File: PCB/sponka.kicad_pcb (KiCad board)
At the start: 2 copper layers, 87.2 x 10.9 mm, 29 parts, among them J1 Conn_01x03_Pin, J2 USB_C_Receptacle_USB2.0_14P, J3 Conn_01x02_Socket, J4 Conn_01x05_Pin, SW1 SW_Push, SW2 SW_SPDT, U1 CH32V003FxUx, U2 TP4057, U3 AP2127K-3.3

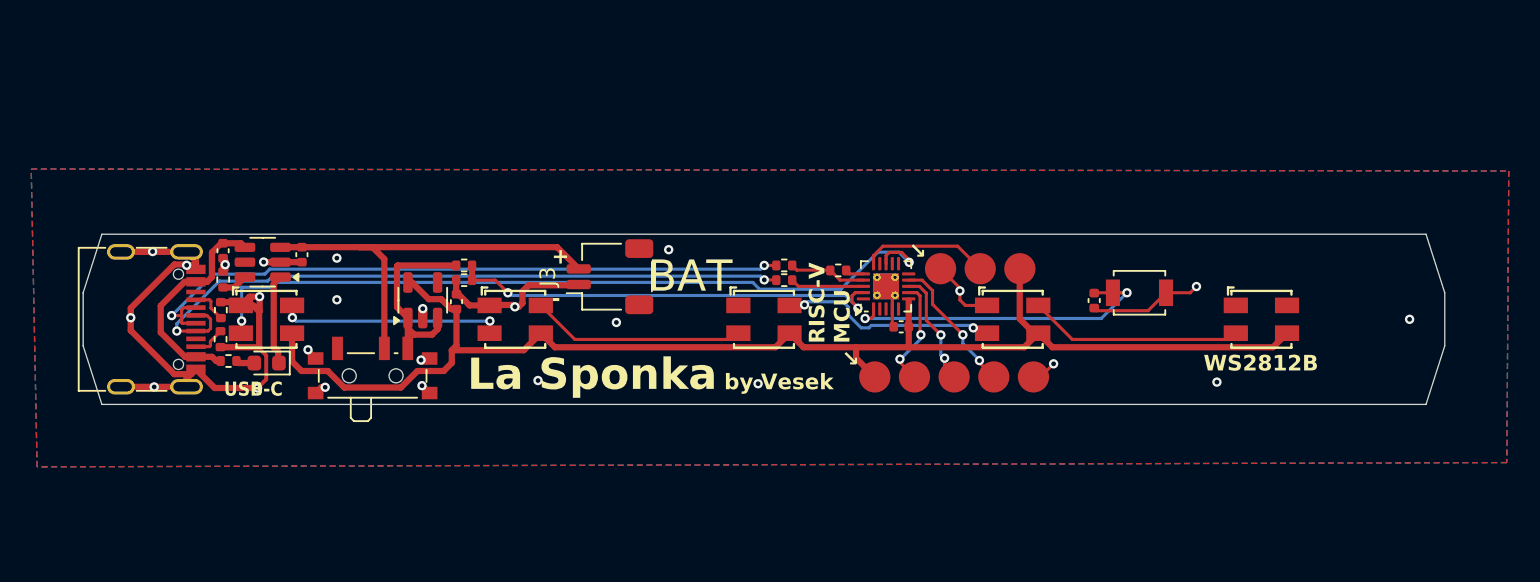
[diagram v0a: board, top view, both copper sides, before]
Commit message: Add protection circuit to PCB I don't like the design tho, so let's fix that
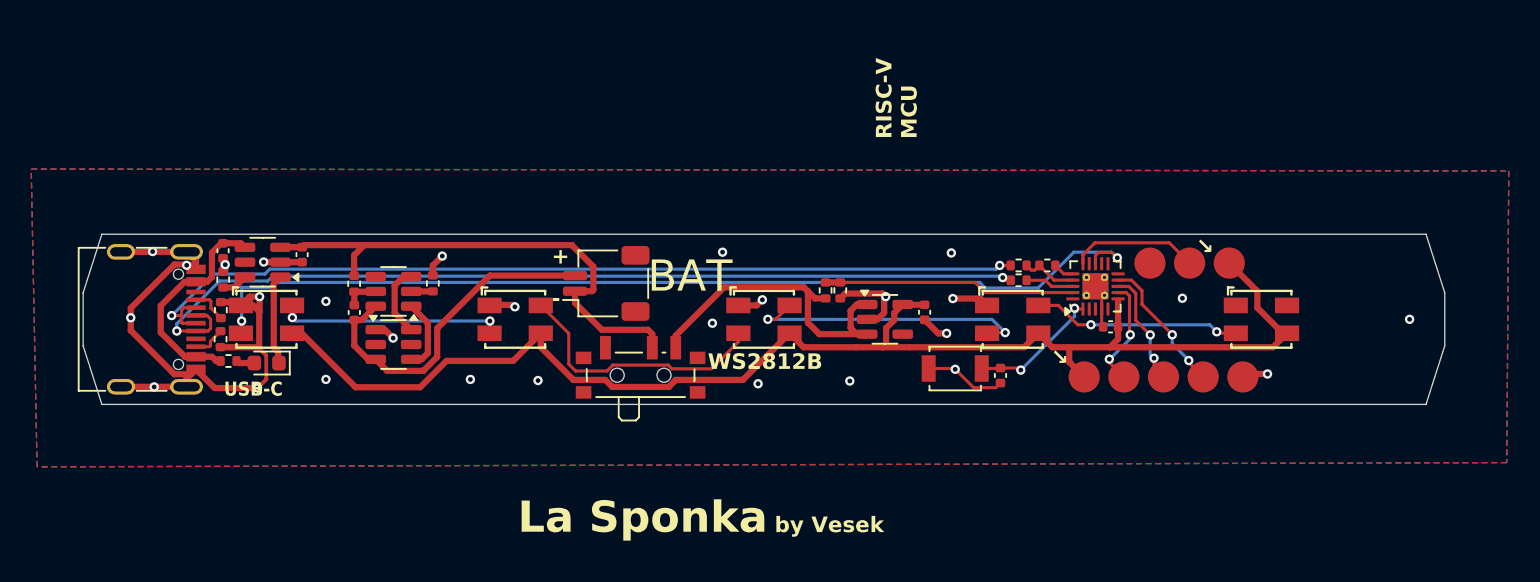
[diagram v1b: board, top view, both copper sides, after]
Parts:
- added C6: 100nF, Capacitor_SMD:C_0402_1005Metric, F.Cu at (118.1, 100.9)
- added Q1: FS8205, Package_TO_SOT_SMD:SOT-23-6, F.Cu at (120.6, 103.0)
- added R10: 100, Resistor_SMD:R_0402_1005Metric, F.Cu at (118.1, 99.1)
- added R11: 1k, Resistor_SMD:R_0402_1005Metric, F.Cu at (123.1, 99.1)
- added U4: DW01A, Package_TO_SOT_SMD:SOT-23-6, F.Cu at (120.6, 99.6)
- moved C5 30.0 mm to (154.6, 100.9), turned to -90 degrees
- moved U3 29.6 mm to (152.1, 101.3), turned to 0 degrees
- moved R8 24.1 mm to (149.2, 99.5), turned to -90 degrees
- moved R7 23.2 mm to (148.2, 99.5), turned to 90 degrees
- moved SW2 17.2 mm to (136.4, 104.6)
- moved R4 15.0 mm to (160.6, 98.8)
- moved R3 15.0 mm to (160.6, 97.9)
- moved J1 13.4 mm to (171.6, 97.8)
- moved C1 13.4 mm to (166.5, 101.8)
- moved J4 13.4 mm to (169.8, 105.0)
- moved U1 13.4 mm to (165.5, 99.2)
- moved R9 13.4 mm to (162.4, 97.9)
- moved SW1 12.8 mm to (156.6, 104.5), turned to 180 degrees
- moved C2 7.68 mm to (159.4, 105.0)
- moved J3 0.49 mm to (134.2, 99.0)
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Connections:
- C4 pad 1: GND -> /Power management/B+
- C4 pad 2: Net-(J3-Pin_2) -> GND
- J3 pad 1: GND -> /Power management/B+
- J3 pad 2: Net-(J3-Pin_2) -> /Power management/B-
- SW2 pad : GND -> (no net)
- SW2 pad 2: Net-(J3-Pin_2) -> /Power management/B+
- U2 pad 3: Net-(J3-Pin_2) -> /Power management/B+
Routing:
- net /Power management/B+: track 0.00 -> 33.0 mm
- net Net-(J3-Pin_2): track 27.3 -> 0.00 mm
- net /Power management/B-: track 0.00 -> 21.8 mm
- net /Power management/DP: track 44.2 -> 59.2 mm
- net /Power management/DN: track 43.4 -> 58.5 mm
- net Net-(U1-PD7): track 21.5 -> 8.51 mm
- net /LED Row/Row_DIN: track 49.7 -> 62.6 mm
- net /Power management/BATT_DIV: track 28.2 -> 16.1 mm, vias 2 -> 0
- net Net-(SW2-C): track 13.0 -> 21.6 mm
- net Net-(Q1-G2): track 0.00 -> 4.67 mm
- net Net-(Q1-G1): track 0.00 -> 4.57 mm
- net Net-(LED3-DOUT): track 14.0 -> 18.5 mm
- net GND: track 77.3 -> 73.1 mm, vias 25 -> 27
- net Net-(LED2-DOUT): track 13.7 -> 17.1 mm
- net Net-(U4-VCC): track 0.00 -> 2.24 mm
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
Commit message: Probably done?
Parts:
- moved LED1 63.7 mm to (176.2, 101.3), turned to 0 degrees
- moved LED5 63.7 mm to (112.5, 101.3), turned to 0 degrees
- moved LED2 31.9 mm to (160.2, 101.3), turned to 0 degrees
- moved LED4 31.9 mm to (128.4, 101.3), turned to 0 degrees
- moved J1 18.9 mm to (152.7, 97.5)
- moved J3 16.6 mm to (118.3, 103.9)
- moved C5 15.2 mm to (139.5, 100.0)
- moved U3 15.2 mm to (136.9, 100.5)
- moved R3 12.8 mm to (148.4, 101.8)
- moved R4 12.8 mm to (148.4, 102.8)
- moved R9 12.8 mm to (150.2, 101.8)
- moved C1 12.7 mm to (154.3, 105.5)
- moved U1 12.7 mm to (153.3, 102.9)
- moved SW1 12.5 mm to (168.8, 102.0), turned to 0 degrees
- moved J4 7.60 mm to (162.2, 105.2)
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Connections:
- SW2 pad : (no net) -> GND
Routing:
- net /Power management/DP: track 59.2 -> 3.98 mm, vias 2 -> 1
- net /Power management/DN: track 58.5 -> 3.39 mm, vias 2 -> 1
- net /LED Row/Row_DIN: track 62.6 -> 26.0 mm
- net GND: track 73.1 -> 58.7 mm, vias 27 -> 23
- net /Power management/BATT_DIV: track 16.1 -> 2.16 mm
- net /Power management/B-: track 21.8 -> 8.89 mm
- net Net-(U1-PD7): track 8.51 -> 20.4 mm
- net +3V3: track 87.8 -> 80.5 mm, vias 0 -> 2
- net Net-(U4-CS): track 1.38 -> 7.90 mm, vias 0 -> 2
- net Net-(D_CHRG1-K): track 5.83 -> 0.00 mm
- net /RTS/SCL: track 9.02 -> 13.8 mm
- net Net-(LED2-DOUT): track 17.1 -> 13.7 mm
- net Net-(J1-Pin_2): track 8.26 -> 5.03 mm, vias 0 -> 2
- net Net-(SW2-C): track 21.6 -> 18.7 mm
- net /RX/SDA: track 7.64 -> 10.4 mm
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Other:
- board text added: "Charging"
- board text added: "RISC-V"
- board text removed: "RISC-V MCU"
- board text removed: "USB-C"

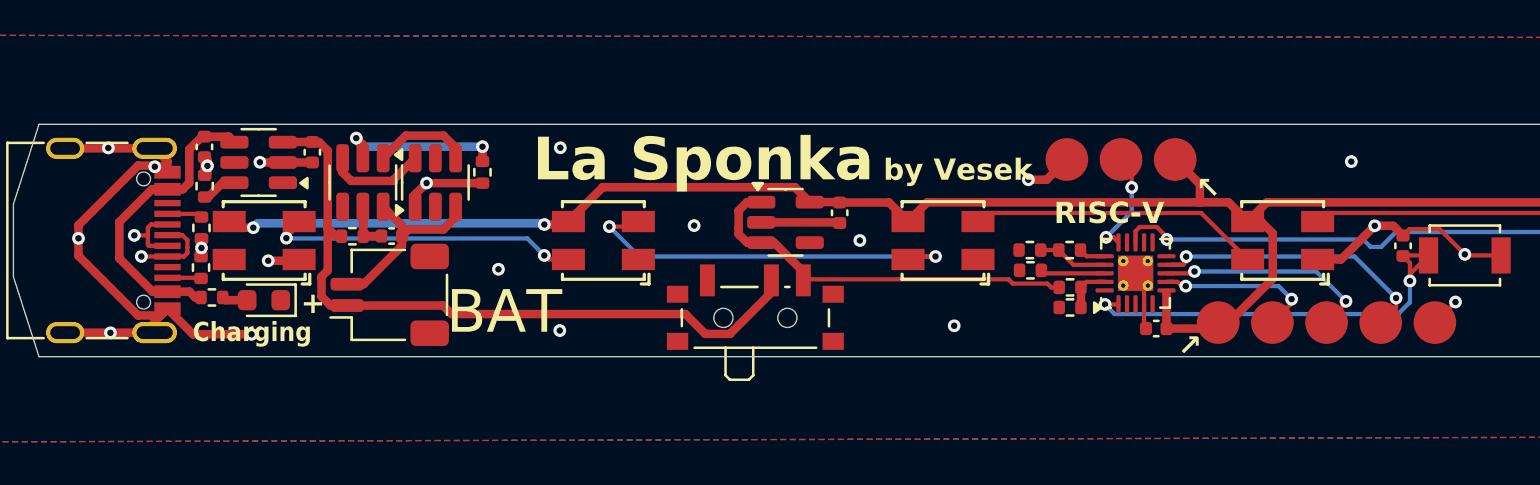
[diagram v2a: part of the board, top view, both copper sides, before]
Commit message: Add USBLC6-2P6 for ESD protection The usual COMPLETE REDESIGN because it didn't fit
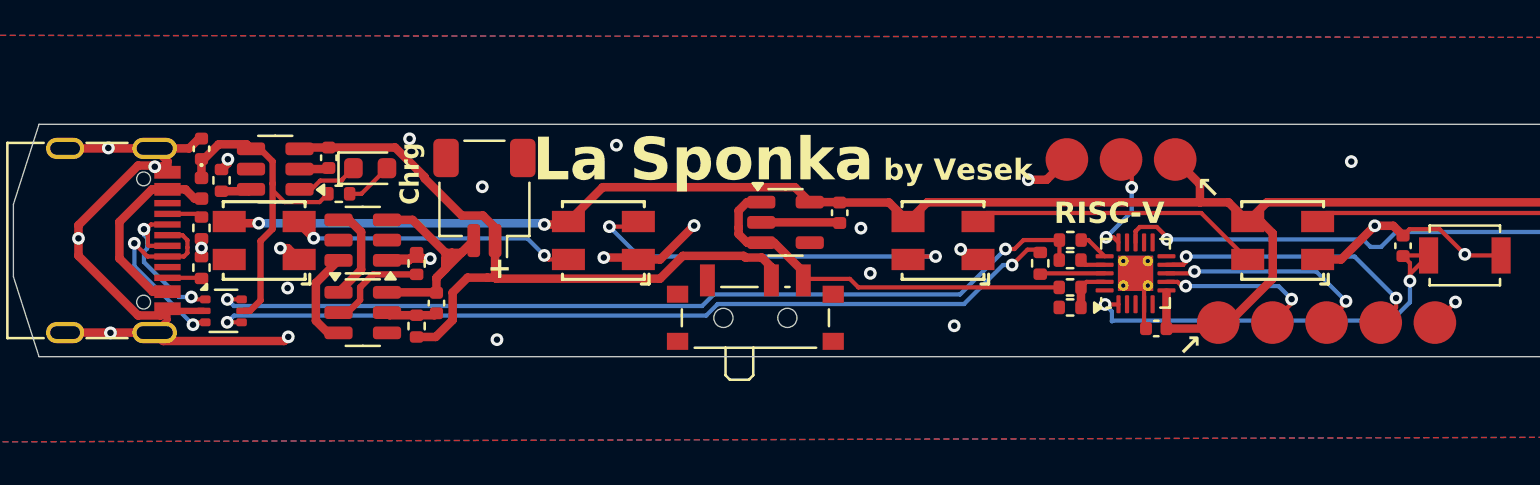
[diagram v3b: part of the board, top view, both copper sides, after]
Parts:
- added D1: D_Schottky, Diode_SMD:D_0402_1005Metric, F.Cu at (109.5, 98.9)
- added U5: USBLC6-2P6, Package_TO_SOT_SMD:SOT-666, F.Cu at (110.5, 104.7)
- J3: value Conn_01x02_Socket -> BAT
- moved D_CHRG1 7.95 mm to (117.4, 98.0), turned to 0 degrees
- moved R5 7.68 mm to (116.0, 99.2)
- moved J3 6.35 mm to (122.8, 99.4), turned to 180 degrees
- moved U4 6.10 mm to (117.1, 104.7), turned to 0 degrees
- moved R11 5.28 mm to (119.6, 102.4), turned to 90 degrees
- moved R10 5.18 mm to (119.6, 105.4), turned to 90 degrees
- moved Q1 4.35 mm to (117.1, 101.3), turned to 180 degrees
- moved C6 3.78 mm to (120.5, 104.3), turned to 90 degrees
- moved R3 1.94 mm to (150.3, 102.3), turned to 0 degrees
- moved U2 0.84 mm to (113.0, 98.0)
- moved R6 0.83 mm to (110.5, 98.5)
- moved C4 0.81 mm to (115.5, 97.5)
- moved R4 0.57 mm to (148.9, 102.4), turned to -90 degrees
- moved R9 0.47 mm to (150.3, 101.3)
- moved C3 0.17 mm to (109.5, 97.0), turned to 90 degrees
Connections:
- net Net-(Q1-G1) renamed /Power management/OC
- net Net-(Q1-G2) renamed /Power management/OD
- net Net-(U4-CS) renamed /Power management/CS
- C3 pad 1: /Power management/VBUS -> +5V
- J2 pad A4: /Power management/VBUS -> VBUS
- J2 pad A9: /Power management/VBUS -> VBUS
- J2 pad B4: /Power management/VBUS -> VBUS
- J2 pad B9: /Power management/VBUS -> VBUS
- J3 pad MP: GND -> (no net)
- R3 pad 2: /Power management/DN -> Net-(U1-PD3)
- R4 pad 2: /Power management/DP -> Net-(U1-PD4)
- R5 pad 1: /Power management/VBUS -> +5V
- SW2 pad : GND -> (no net)
- U1 pad 17: /Power management/USB_DN -> Net-(U1-PD3)
- U1 pad 18: /Power management/USB_DP -> Net-(U1-PD4)
- U2 pad 4: /Power management/VBUS -> +5V
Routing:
- net /Power management/USB_DN: track 3.28 -> 42.0 mm, vias 0 -> 2
- net /Power management/USB_DP: track 3.00 -> 40.3 mm, vias 0 -> 2
- net +5V: track 0.00 -> 15.9 mm
- net /Power management/VBUS: track 14.4 -> 0.00 mm
- net GND: track 58.7 -> 68.5 mm, vias 23 -> 26
- net VBUS: track 0.00 -> 9.28 mm
- net /Power management/DP: track 3.98 -> 10.0 mm, vias 1 -> 2
- net /Power management/DN: track 3.39 -> 8.36 mm, vias 1 -> 2
- net /Power management/B-: track 8.89 -> 12.4 mm
- net /Power management/CS: track 7.90 -> 4.75 mm, vias 2 -> 0
- net Net-(U1-PD4): track 0.00 -> 3.04 mm
- net Net-(D_CHRG1-K): track 0.00 -> 2.95 mm
- net Net-(LED4-DOUT): track 14.7 -> 13.4 mm
- net Net-(U1-PD3): track 0.00 -> 1.20 mm
- net Net-(D_CHRG1-A): track 1.20 -> 2.25 mm
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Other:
- board text added: "Chrg"
- board text removed: "BAT"
- board text removed: "Charging"

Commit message: Replace 5k with 5.1k resistor Resistor for limiting charging current, it is within tolerance - eliminating one SKU
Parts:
- R6: value 5k -> 5.1k
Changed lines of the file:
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@@
 		(tags "SOT-666")
 		(property "Reference" "U5"
-			(at 0 -2 360)
+			(at 0 -2 0)
 			(layer "F.SilkS")
 			(hide yes)
@@
 		)
 		(property "Value" "USBLC6-2P6"
-			(at 0 1.75 360)
+			(at 0 1.75 0)
 			(layer "F.Fab")
 			(effects
@@
 			)
 		)
-		(property "Value" "5k"
+		(property "Value" "5.1k"
 			(at 0 1.17 90)
 			(layer "F.Fab")
@@
 		(tags "SOT TO_SOT_SMD")
 		(property "Reference" "U4"
-			(at 0 -2.4 360)
+			(at 0 -2.4 0)
 			(layer "F.SilkS")
 			(hide yes)
@@
 		)
 		(property "Value" "DW01A"
-			(at 0 2.4 360)
+			(at 0 2.4 0)
 			(layer "F.Fab")
 			(effects
@@
 		)
 		(fp_text user "${REFERENCE}"
-			(at 0 0 360)
+			(at 0 0 0)
 			(layer "F.Fab")
 			(effects
@@
 		(tags "resistor")
 		(property "Reference" "R3"
-			(at 0 -1.17 360)
+			(at 0 -1.17 0)
 			(layer "F.SilkS")
 			(hide yes)
@@
 		)
 		(property "Value" "33"
-			(at 0 1.17 360)
+			(at 0 1.17 0)
 			(layer "F.Fab")
 			(effects
@@
 		)
 		(fp_text user "${REFERENCE}"
-			(at 0 0 360)
+			(at 0 0 0)
 			(layer "F.Fab")
 			(effects
@@
 		(tags "LED")
 		(property "Reference" "D_CHRG1"
-			(at 0 -1.43 360)
+			(at 0 -1.43 0)
 			(layer "F.SilkS")
 			(hide yes)
@@
 		)
 		(property "Value" "LED"
-			(at 0 1.43 360)
+			(at 0 1.43 0)
 			(layer "F.Fab")
 			(effects
@@
 		)
 		(fp_text user "${REFERENCE}"
-			(at 0 0 360)
+			(at 0 0 0)
 			(layer "F.Fab")
 			(effects
@@
 		(tags "SOT TO_SOT_SMD")
 		(property "Reference" "Q1"
-			(at 0 -2.4 360)
+			(at 0 -2.4 0)
 			(layer "F.SilkS")
 			(hide yes)
@@
 		)
 		(property "Value" "FS8205"
-			(at 0 2.4 360)
+			(at 0 2.4 0)
 			(layer "F.Fab")
 			(effects
@@
 		)
 		(fp_text user "${REFERENCE}"
-			(at 0 0 360)
+			(at 0 0 0)
 			(layer "F.Fab")
 			(effects
@@
 		(tags "connector JST SH horizontal")
 		(property "Reference" "J3"
-			(at 0 -3.98 360)
+			(at 0 -3.98 0)
 			(layer "F.SilkS")
 			(hide yes)
@@
 		)
 		(property "Value" "BAT"
-			(at 0 3.98 360)
+			(at 0 3.98 0)
 			(layer "F.Fab")
 			(effects
@@
 		)
 		(fp_text user "${REFERENCE}"
-			(at 0 0 360)
+			(at 0 0 0)
 			(layer "F.Fab")
 			(effects
@@
 		(tags "resistor")
 		(property "Reference" "R5"
-			(at 0 -1.17 360)
+			(at 0 -1.17 0)
 			(layer "F.SilkS")
 			(hide yes)
@@
 		)
 		(property "Value" "2.2k"
-			(at 0 1.17 360)
+			(at 0 1.17 0)
 			(layer "F.Fab")
 			(effects
@@
 		)
 		(fp_text user "${REFERENCE}"
-			(at 0 0 360)
+			(at 0 0 0)
 			(layer "F.Fab")
 			(effects

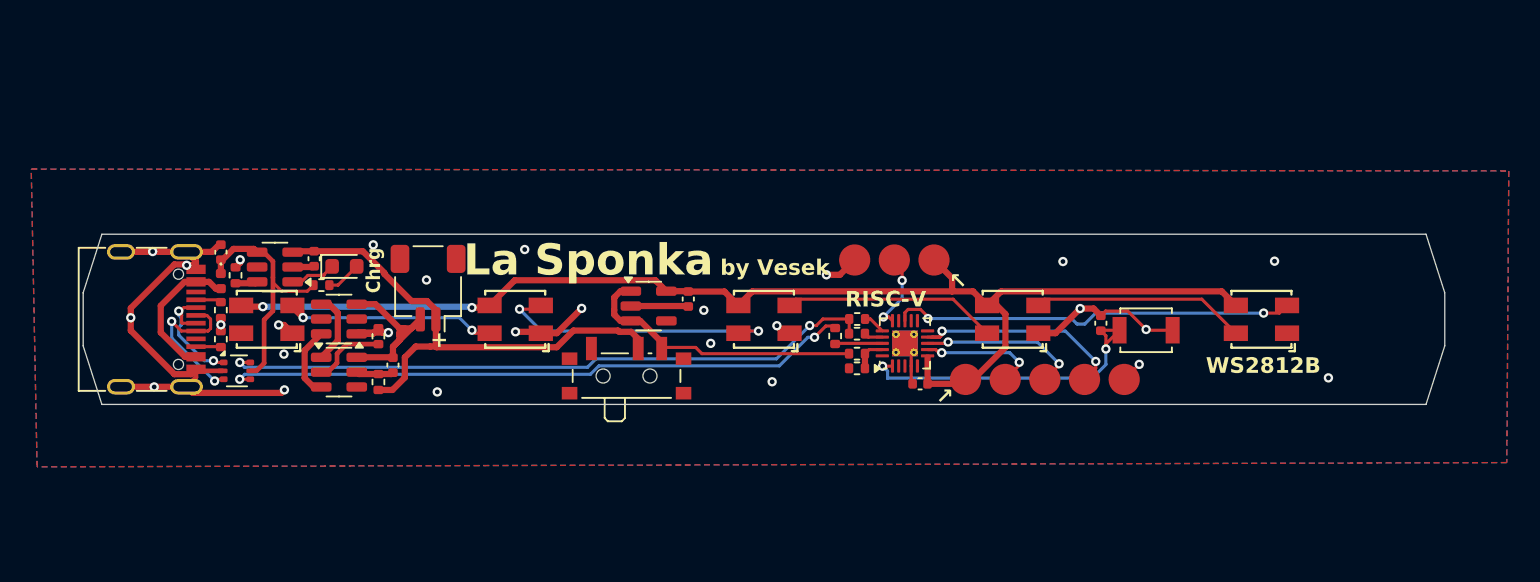
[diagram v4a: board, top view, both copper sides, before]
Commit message: Small polishing touches Move vias out of the way of silkscreen and vice versa
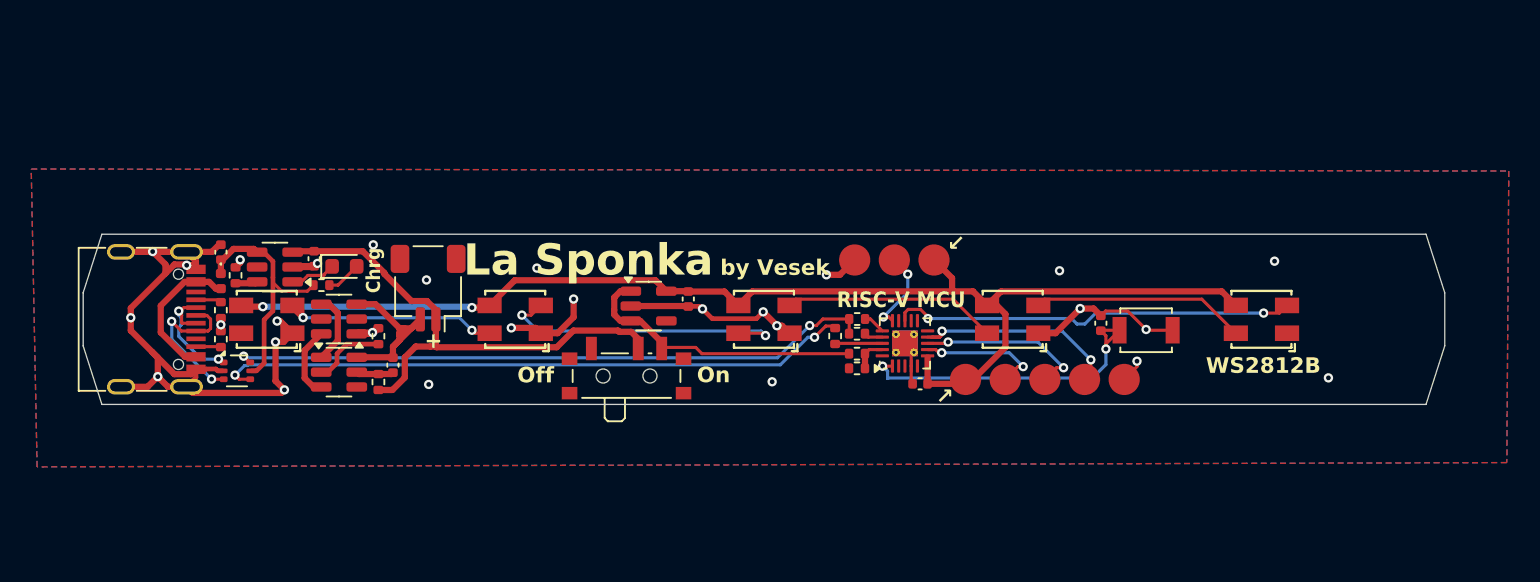
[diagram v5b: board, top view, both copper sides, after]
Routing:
- net GND: track 68.5 -> 85.3 mm, vias 26 -> 28
- net Net-(LED3-DOUT): track 18.7 -> 19.4 mm
- net /Power management/USB_DN: track 42.0 -> 41.4 mm
- net /Power management/USB_DP: track 40.3 -> 40.9 mm
- net /RX/SDA: track 10.4 -> 10.9 mm
- net (no net): vias 1 -> 0
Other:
- board text added: "Off"
- board text added: "On"
- board text added: "RISC-V MCU"
- board text removed: "RISC-V"

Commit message: Change LED resistor value
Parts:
- D_CHRG1: value LED -> RED_LED
- R5: value 2.2k -> 1.5k
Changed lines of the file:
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@@
 			(layer "F.SilkS"
 				(type "Top Silk Screen")
+				(color "White")
+				(material "Direct Printing")
 			)
 			(layer "F.Paste"
@@
 			(layer "F.Mask"
 				(type "Top Solder Mask")
-				(color "Yellow")
+				(color "#DD8500CC")
 				(thickness 0.0275)
 			)
@@
 			(layer "B.Mask"
 				(type "Bottom Solder Mask")
-				(color "Yellow")
+				(color "#DD8500CC")
 				(thickness 0.0275)
 			)
@@
 			(layer "B.SilkS"
 				(type "Bottom Silk Screen")
+				(color "White")
+				(material "Direct Printing")
 			)
 			(copper_finish "None")
@@
 			)
 		)
-		(property "Value" "LED"
+		(property "Value" "RED_LED"
 			(at 0 1.43 0)
 			(layer "F.Fab")
@@
 			)
 		)
-		(property "Value" "2.2k"
+		(property "Value" "1.5k"
 			(at 0 1.17 0)
 			(layer "F.Fab")
